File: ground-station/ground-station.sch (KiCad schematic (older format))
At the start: 27 parts, among them J1 Conn_01x02, J10 Conn_01x02, J2 Conn_01x02, J3 Conn_01x02, J4 Conn_01x02, J5 Conn_01x05, J6 Conn_01x04, J7 USB_B_Micro, J8 Conn_01x02, J9 Conn_01x02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

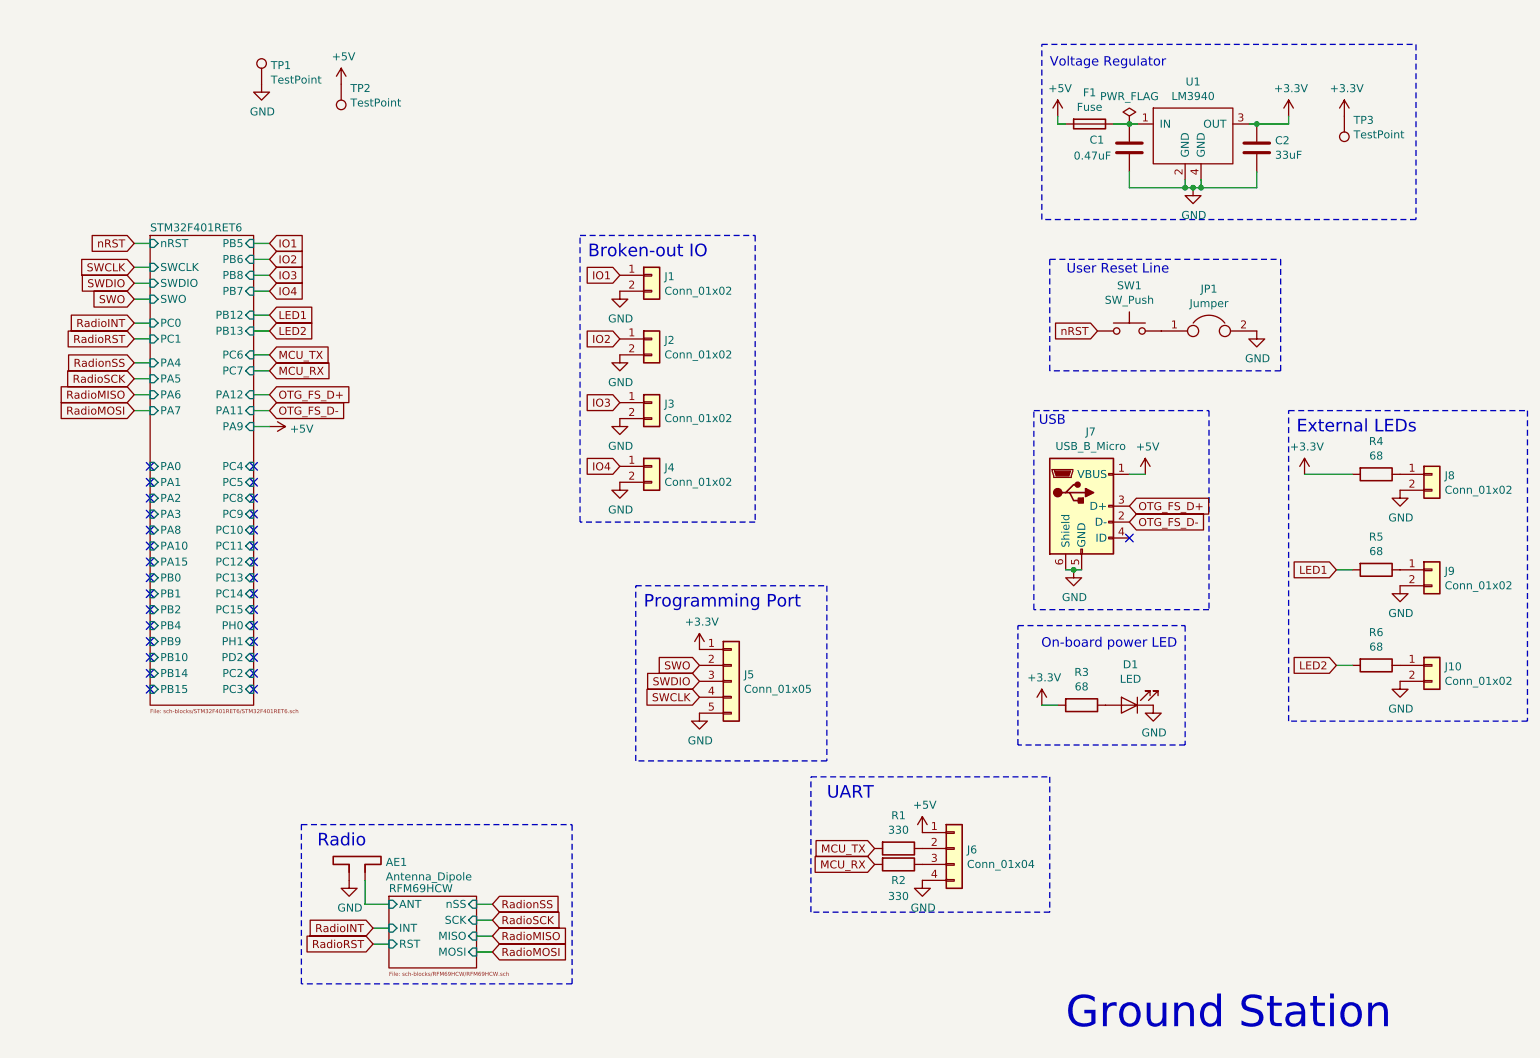
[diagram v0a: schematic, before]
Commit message: added test points and organized schematic
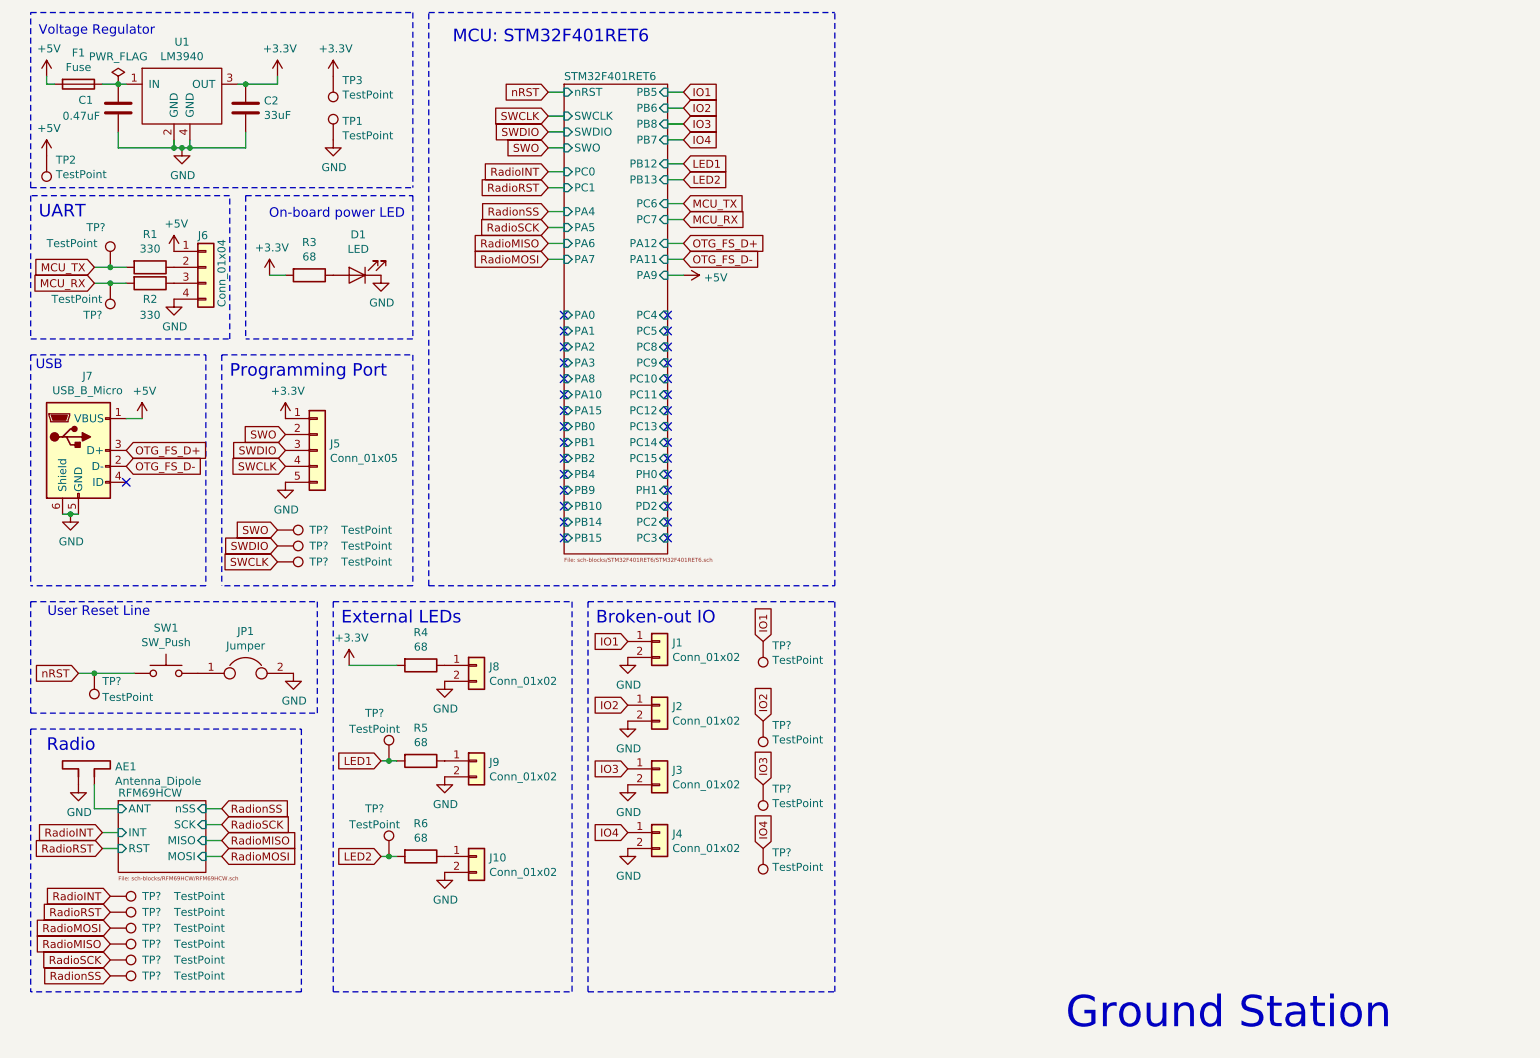
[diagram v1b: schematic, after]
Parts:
- added TP? (x18): TestPoint, symbol Connector:TestPoint
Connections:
- net IO1: now also TP?.1
- net IO2: now also TP?.1
- net IO3: now also TP?.1
- net IO4: now also TP?.1
- net LED1: now also TP?.1
- net LED2: now also TP?.1
- net MCU_RX: now also TP?.1
- net MCU_TX: now also TP?.1
- net RadioINT: now also TP?.1
- net RadioMISO: now also TP?.1
- net RadioMOSI: now also TP?.1
- net RadioRST: now also TP?.1
- net RadioSCK: now also TP?.1
- net RadionSS: now also TP?.1
- net SWCLK: now also TP?.1
- net SWDIO: now also TP?.1
- net SWO: now also TP?.1
- net nRST: now also TP?.1
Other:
- note added: "MCU: STM32F401RET6"
- moved on the sheet: AE1, C1, C2, D1, F1, J1, J10, J2, J3, J4, J5, J6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

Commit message: created footprints for rfm, usb micro b, and sma, and assigned all footprints
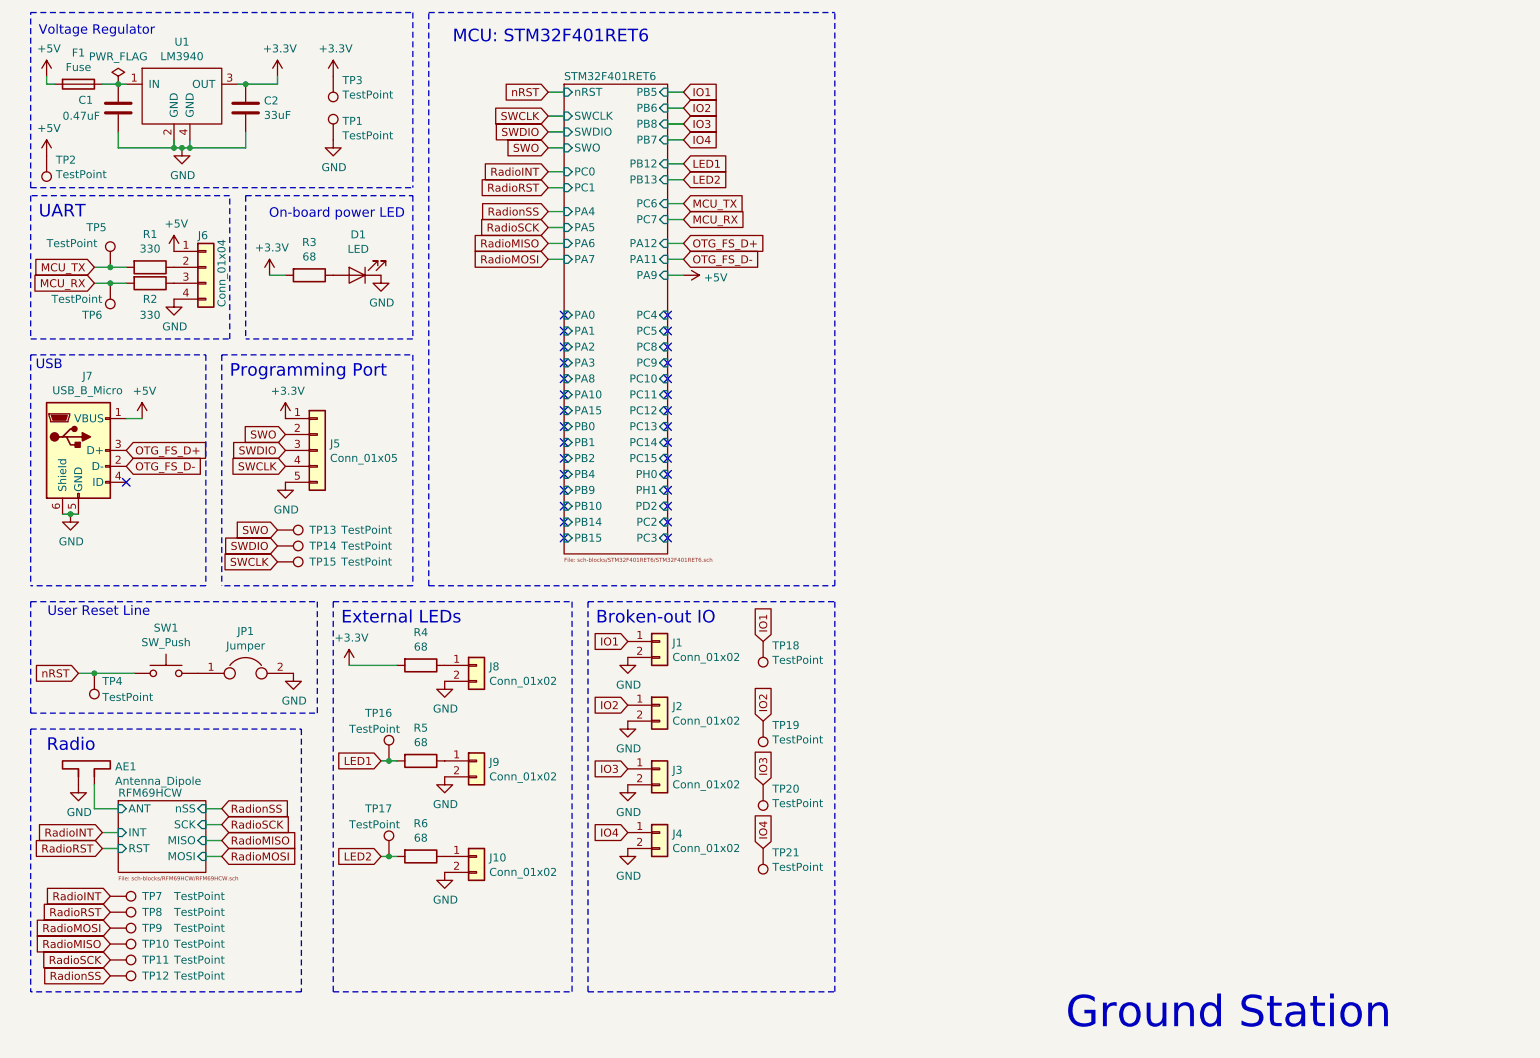
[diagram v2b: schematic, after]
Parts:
- AE1: footprint (none) -> Connector_Coaxial:SMA_Molex_73251-1153_EdgeMount_Horizontal
- C1, C2: footprint (none) -> Capacitor_SMD:C_0603_1608Metric_Pad1.05x0.95mm_HandSolder
- D1: footprint (none) -> LED_SMD:LED_0603_1608Metric_Pad1.05x0.95mm_HandSolder
- F1: footprint (none) -> Fuse:Fuse_0603_1608Metric_Pad1.05x0.95mm_HandSolder
- J1, J10, J2, J3, J4, J8, J9: footprint (none) -> calstar:Molex_Micro-Lock_505568-0271_1x02_P1.25mm_Vertical
- J5: footprint (none) -> Connector_PinHeader_2.54mm:PinHeader_1x05_P2.54mm_Vertical
- J6: footprint (none) -> Connector_PinHeader_2.54mm:PinHeader_1x04_P2.54mm_Vertical
- J7: footprint (none) -> calstar:USB_Micro-B_Amphenol_10118192-0001LF_Horizontal
- JP1: footprint (none) -> Connector_PinHeader_2.54mm:PinHeader_1x02_P2.54mm_Vertical
- R1, R2, R3, R4, R5, R6: footprint (none) -> Resistor_SMD:R_0603_1608Metric_Pad1.05x0.95mm_HandSolder
- SW1: footprint (none) -> Button_Switch_THT:SW_PUSH_6mm
- TP1, TP2, TP3: footprint (none) -> TestPoint:TestPoint_THTPad_1.0x1.0mm_Drill0.5mm
- TP10, TP11, TP12, TP13, TP14, TP15, TP16, TP17, TP18, TP19, TP20, TP21, TP4, TP5, TP6, TP7, TP8, TP9: renamed from TP?; footprint (none) -> TestPoint:TestPoint_THTPad_1.0x1.0mm_Drill0.5mm

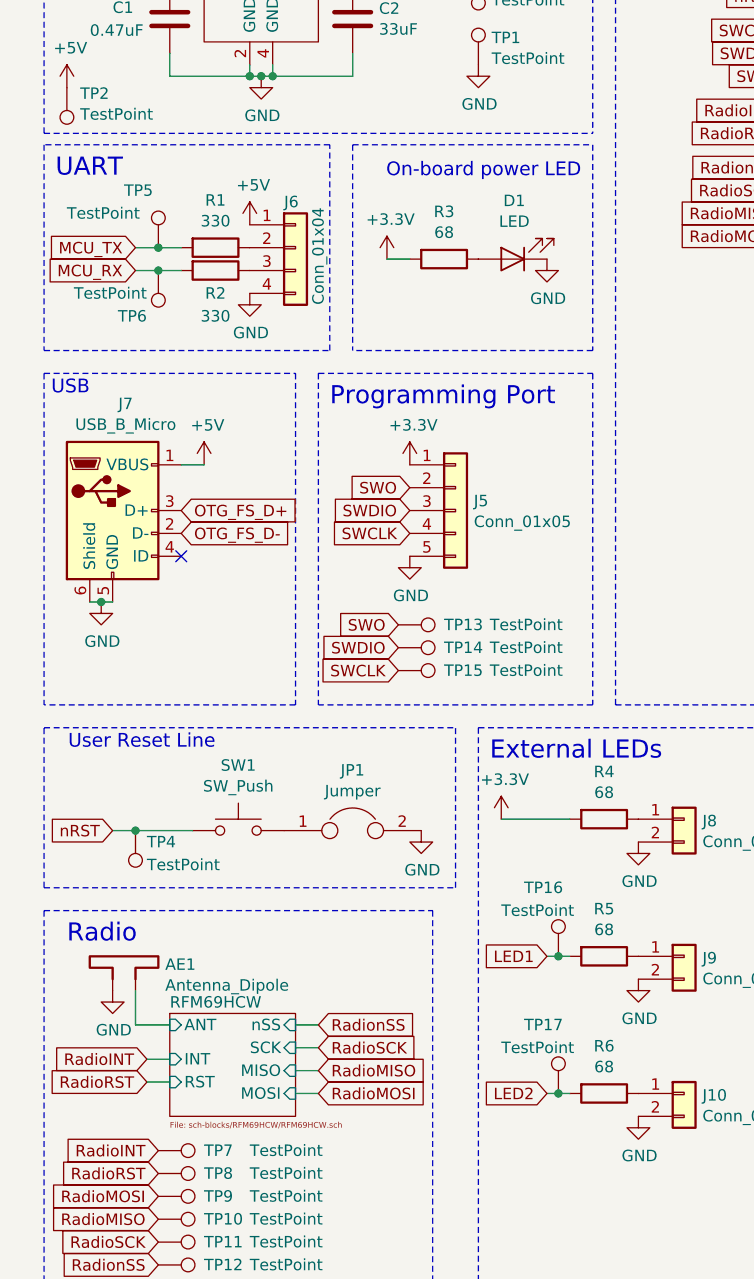
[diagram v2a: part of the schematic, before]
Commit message: lots of work on layout + change button to compact button
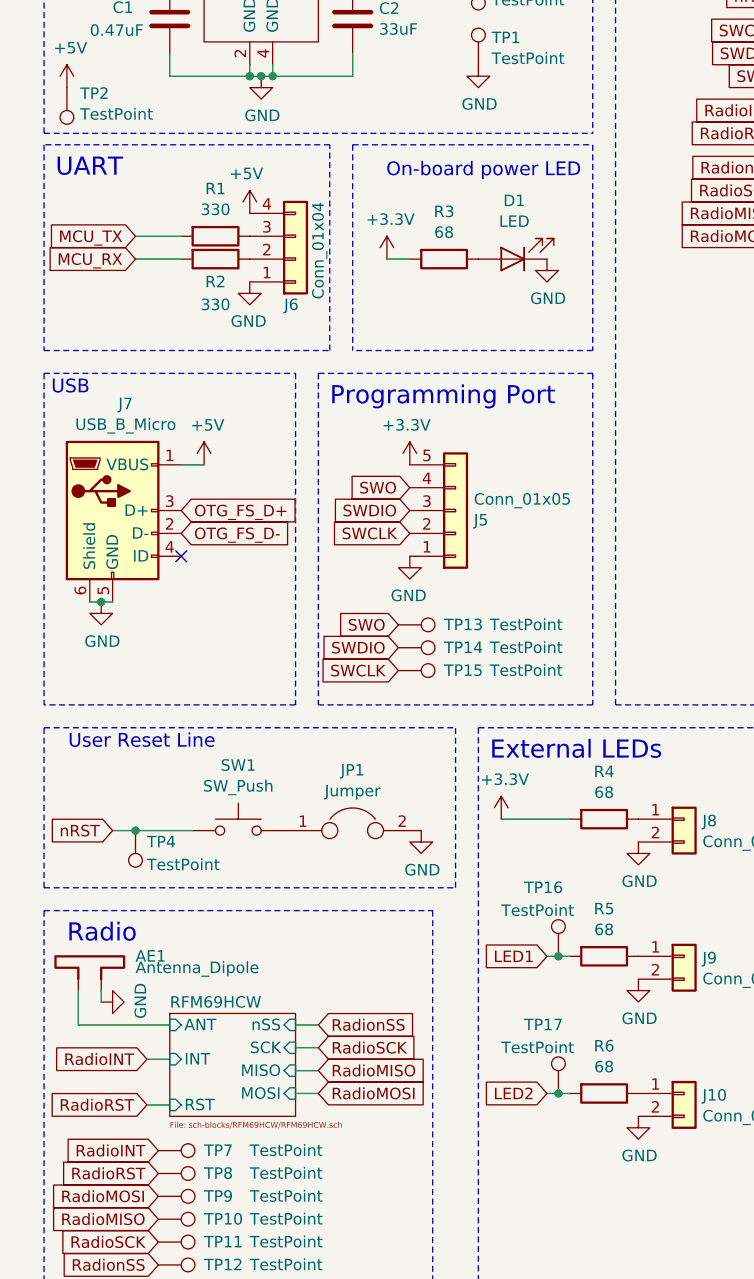
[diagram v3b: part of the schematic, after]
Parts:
- removed TP5, TP6: TestPoint, TestPoint:TestPoint_THTPad_1.0x1.0mm_Drill0.5mm, symbol Connector:TestPoint
- SW1: footprint Button_Switch_THT:SW_PUSH_6mm -> calstar:TE_Button_USLPT3026
- TP1, TP10, TP11, TP12, TP13, TP14, TP15, TP16, TP17, TP18, TP19, TP2, TP20, TP21, TP3, TP4, TP7, TP8, TP9: footprint TestPoint:TestPoint_THTPad_1.0x1.0mm_Drill0.5mm -> TestPoint:TestPoint_THTPad_D1.0mm_Drill0.5mm
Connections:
- net +3V3: now also J5.5 (Pin_5); no longer J5.1 (Pin_1)
- net +5V: now also J6.4 (Pin_4); no longer J6.1 (Pin_1)
- net GND: now also AE1.2, J5.1 (Pin_1), J6.1 (Pin_1); no longer AE1.1, J5.5 (Pin_5), J6.4 (Pin_4)
- net RFM69HCW/ANT: now also AE1.1; no longer AE1.2
- net SWCLK: now also J5.2 (Pin_2); no longer J5.4 (Pin_4)
- net SWO: now also J5.4 (Pin_4); no longer J5.2 (Pin_2)
- net at J6.2 (Pin_2): now also R2.1; no longer R1.1
- net at J6.3 (Pin_3): now also R1.1; no longer R2.1
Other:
- moved on the sheet: AE1, J6, R1, R2
